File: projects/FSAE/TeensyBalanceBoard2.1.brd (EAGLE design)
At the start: 165.1 x 63.2 mm, 137 parts

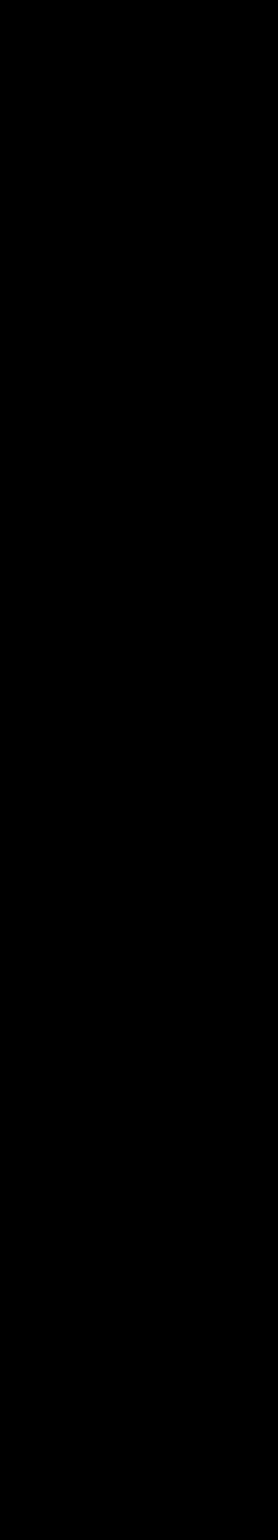
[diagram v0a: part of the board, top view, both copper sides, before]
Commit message: added 18650 holder
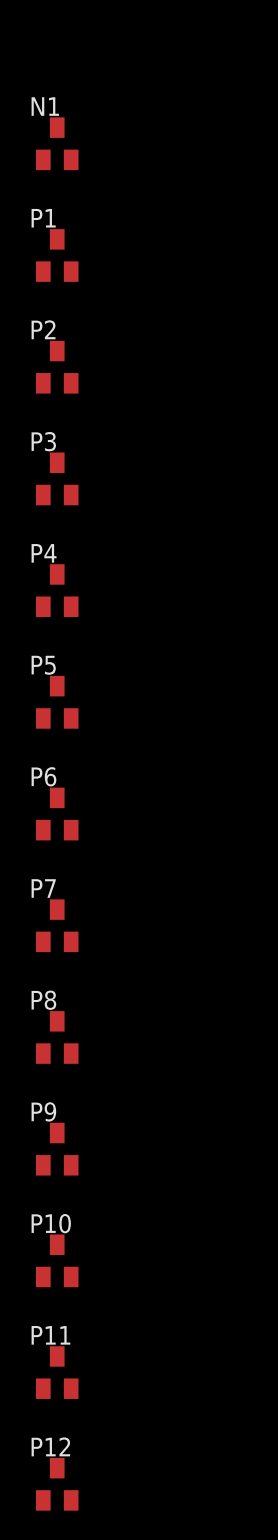
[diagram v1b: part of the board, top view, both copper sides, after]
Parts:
- added N1: BSS123, transistor-small-signal:SOT23
- added P1, P10, P11, P12, P2, P3, P4, P5, P6, P7, P8, P9: BSS84, transistor-small-signal:SOT23
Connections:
- new net BGND: BAT_TERMINALS.1, N1.2
- new net BT1: BAT_TERMINALS.2, P1.3
- new net BT10: BAT_TERMINALS.11
- new net BT11: BAT_TERMINALS.12
- new net BT12: BAT_TERMINALS.13
- new net BT2: BAT_TERMINALS.3
- new net BT3: BAT_TERMINALS.4
- new net BT4: BAT_TERMINALS.5
- new net BT5: BAT_TERMINALS.6
- new net BT6: BAT_TERMINALS.7
- new net BT7: BAT_TERMINALS.8
- new net BT8: BAT_TERMINALS.9
- new net BT9: BAT_TERMINALS.10
- new net N$47: P1.2, RBH1.2
- net 5V: now also N1.1
- net AGND: now also N1.3, P1.1; no longer BAT_TERMINALS.13
- net B1: no longer BAT_TERMINALS.12, RBH1.2
- net B10: no longer BAT_TERMINALS.3, RBH10.2
- net B11: no longer BAT_TERMINALS.2, RBH11.2
- net B12: no longer BAT_TERMINALS.1, RBH12.2
- net B2: no longer BAT_TERMINALS.11, RBH2.2
- net B3: no longer BAT_TERMINALS.10, RBH3.2
- net B4: no longer BAT_TERMINALS.9, RBH4.2
- net B5: no longer BAT_TERMINALS.8, RBH5.2
- net B6: no longer BAT_TERMINALS.7, RBH6.2
- net B7: no longer BAT_TERMINALS.6, RBH7.2
- net B8: no longer BAT_TERMINALS.5, RBH8.2
- net B9: no longer BAT_TERMINALS.4, RBH9.2
